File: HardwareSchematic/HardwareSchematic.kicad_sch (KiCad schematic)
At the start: 10 parts, among them U1 24C32 EEPROM

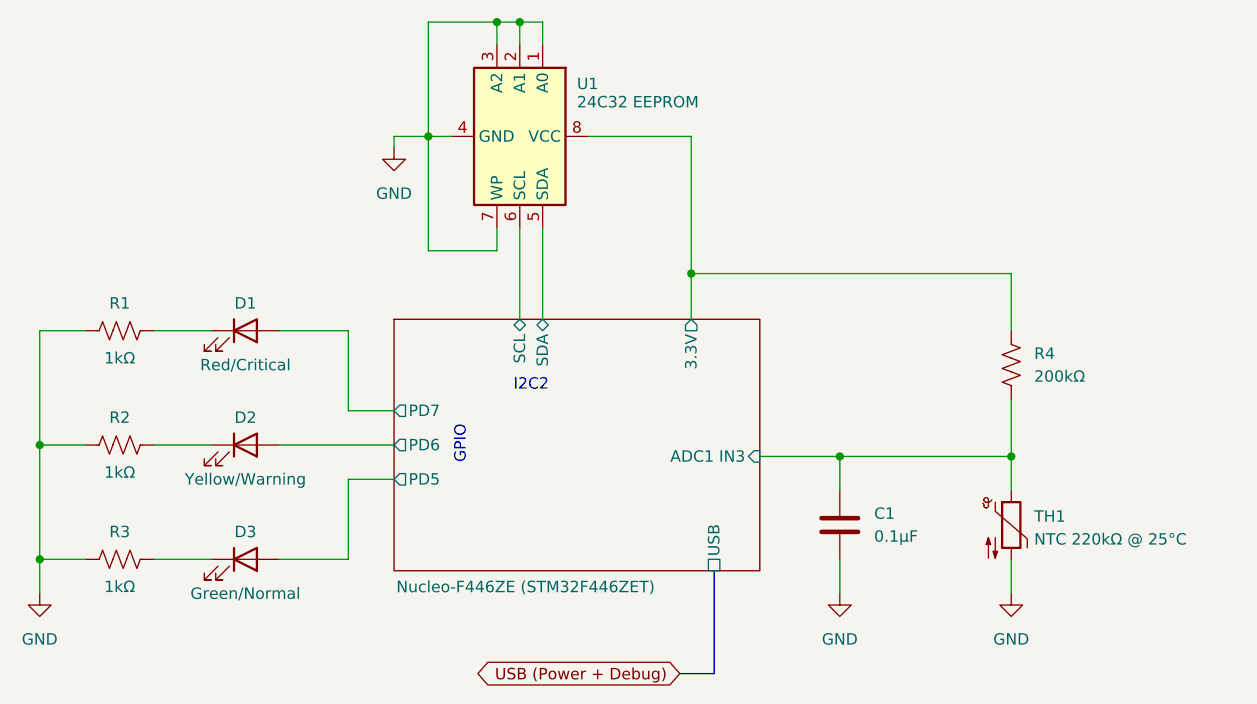
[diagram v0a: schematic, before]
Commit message: Hardware documentation: Added missing components
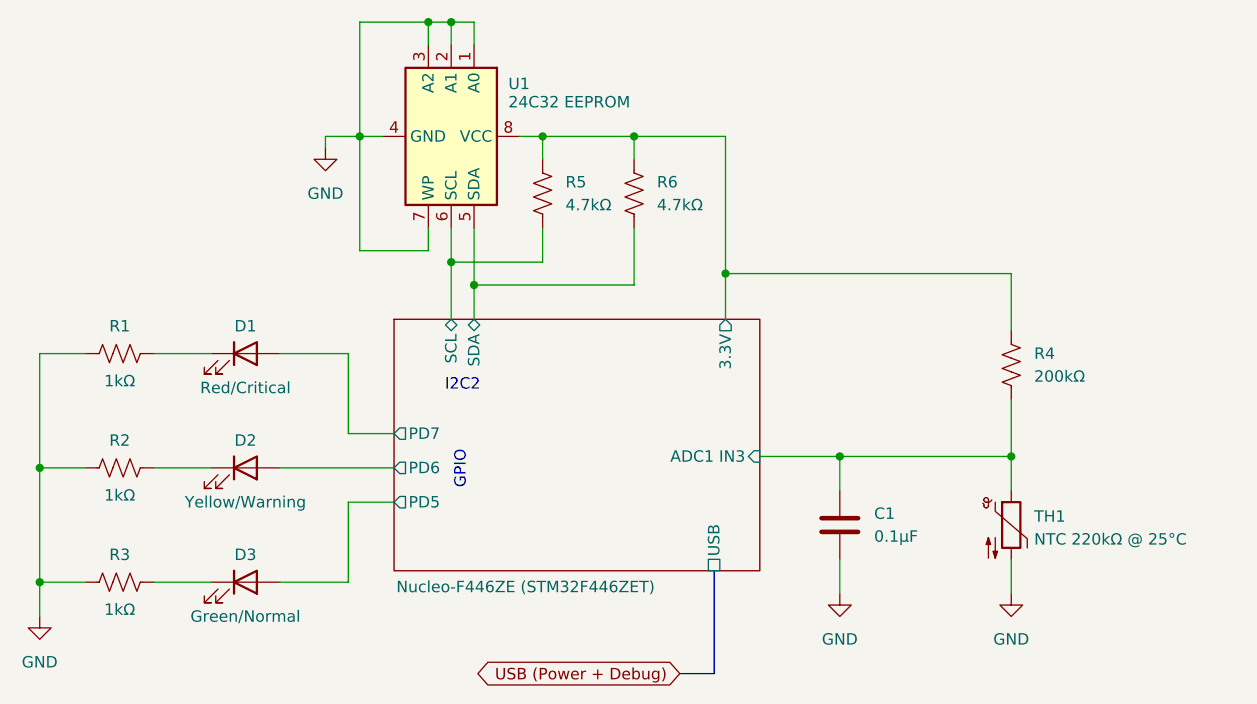
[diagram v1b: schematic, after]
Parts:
- added R5, R6: 4.7kΩ, symbol Device:R_US
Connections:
- net Nucleo-F446ZE (STM32F446ZET)/3.3V: now also R5.2, R6.2
- net Nucleo-F446ZE (STM32F446ZET)/SCL: now also R5.1
- net Nucleo-F446ZE (STM32F446ZET)/SDA: now also R6.1
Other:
- moved on the sheet: D1, D2, D3, R1, R2, R3, U1
